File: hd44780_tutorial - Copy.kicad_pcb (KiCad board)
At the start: 2 copper layers, 157.2 x 83.5 mm, 33 parts, among them J1 LCD_2004_PinSocket_1x16_P2.54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, J2 UJC-HP-3-SMT-TR, SW1 REG SELECT, SW2 ENABLE, SW3 DS02C-254-1L-08BE

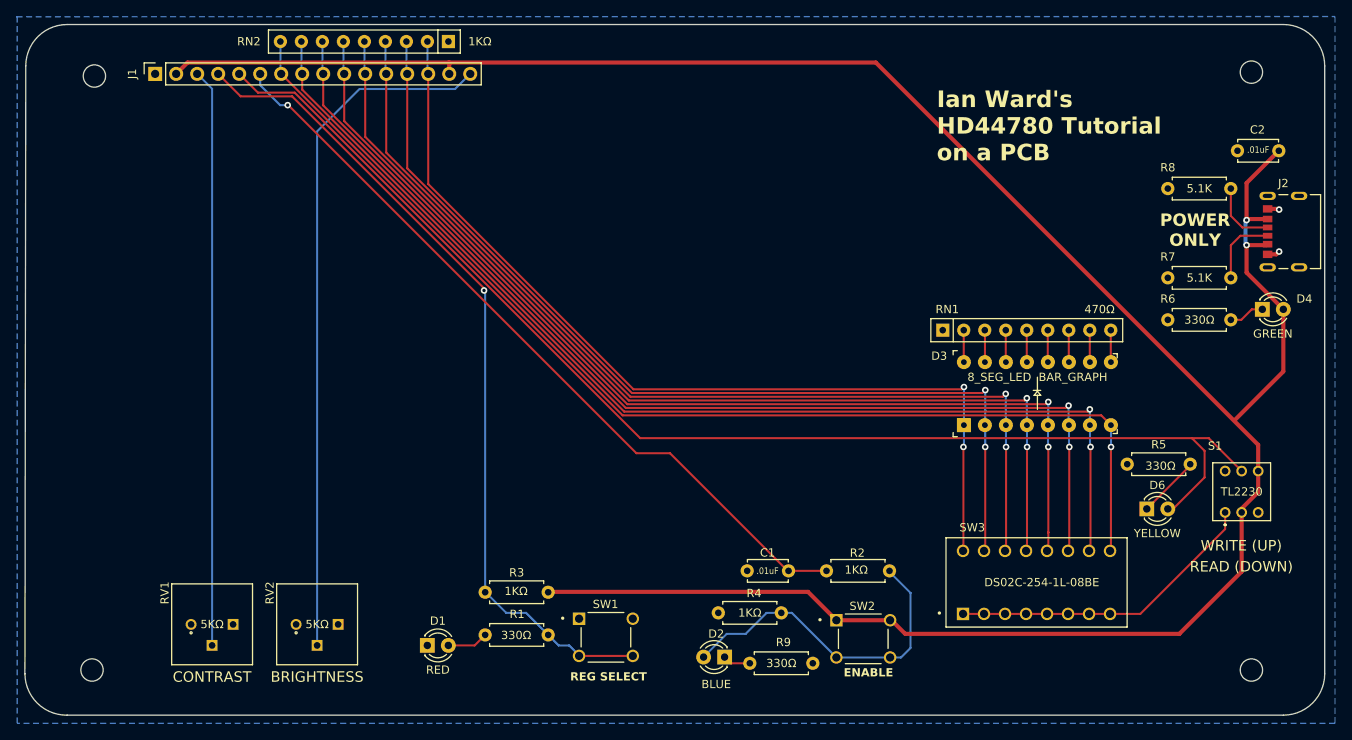
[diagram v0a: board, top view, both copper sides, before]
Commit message: Determined that adding 1K resistor to SW2 fixes the problem with this board. Created new gerber/drill files.
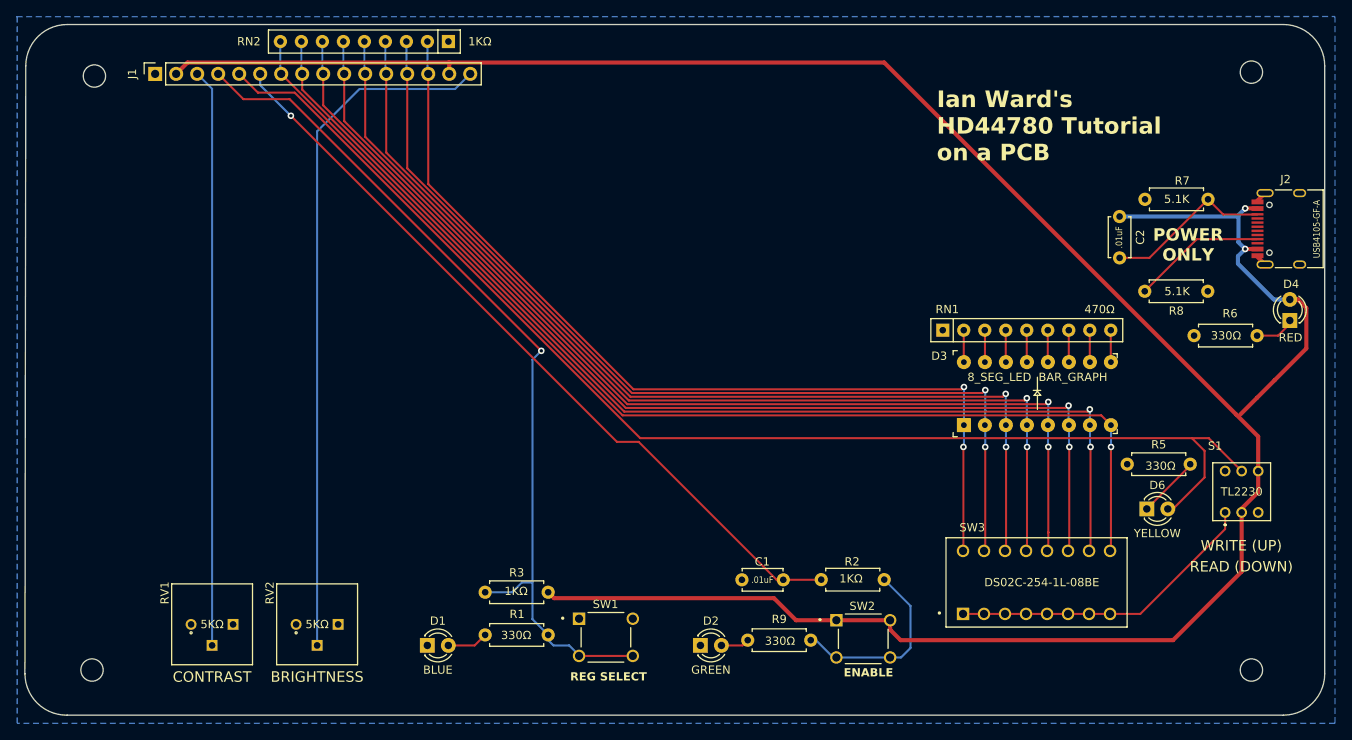
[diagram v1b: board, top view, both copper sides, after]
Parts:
- removed R4: 1KΩ, Resistor_THT:R_Axial_DIN0207_L6.3mm_D2.5mm_P7.62mm_Horizontal
- D1: value RED -> BLUE
- D2: value BLUE -> GREEN
- D4: value GREEN -> RED
- J2: value UJC-HP-3-SMT-TR -> USB4105-GF-A; footprint Lutzcraft:CUI_UJC-HP-3-SMT-TR -> footprints:USB_C_Receptacle_HRO_TYPE-C-31-M-12
- moved C2 20.8 mm to (193.6, 69.4), turned to -90 degrees
- moved R8 12.7 mm to (204.2, 78.5)
- moved R7 9.89 mm to (204.2, 67.3)
- moved R9 7.88 mm to (156.2, 120.7), turned to 180 degrees
- moved R6 3.70 mm to (202.6, 83.8)
- moved D4 3.59 mm to (214.1, 82.0), turned to 90 degrees
- moved D2 3.25 mm to (142.9, 121.3), turned to 0 degrees
- moved REF** 3.02 mm to (124.5, 80.0)
- moved J2 2.84 mm to (214.3, 70.9)
- moved C1 1.25 mm to (152.9, 113.3)
- moved R2 1.24 mm to (165.1, 113.3)
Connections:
- C2 pad 2: GND -> Net-(C2-Pad2)
- D2 pad 1: Net-(D2-K) -> GND
- J2 pad A5: Net-(J2-CC1) -> Net-(J2-PadA5)
- J2 pad B5: Net-(J2-CC2) -> Net-(C2-Pad2)
- J2 pad S1: unconnected-(J2-SHIELD-PadS1) -> GND
- R2 pad 1: Net-(D2-A) -> Net-(R2-Pad1)
- R7 pad 1: Net-(J2-CC1) -> Net-(C2-Pad2)
- R8 pad 1: Net-(J2-CC2) -> GND
- R8 pad 2: GND -> Net-(J2-PadA5)
- R9 pad 1: Net-(D2-K) -> Net-(R2-Pad1)
- R9 pad 2: GND -> Net-(D2-A)
- SW2 pad 3: Net-(D2-A) -> Net-(R2-Pad1)
- SW2 pad 4: Net-(D2-A) -> Net-(R2-Pad1)
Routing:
- net Net-(D2-A): track 40.3 -> 3.45 mm
- net Net-(R2-Pad1): track 0.00 -> 23.0 mm
- net Net-(C2-Pad2): track 0.00 -> 20.3 mm
- net Net-(J2-PadA5): track 0.00 -> 16.2 mm
- net +5V: track 300.9 -> 311.6 mm
- net Net-(J2-CC1): track 8.86 -> 0.00 mm
- net Net-(J2-CC2): track 8.33 -> 0.00 mm
- net /RS: track 100.8 -> 106.4 mm
- net Net-(D2-K): track 3.36 -> 0.00 mm
- net Net-(D4-K): track 4.34 -> 4.96 mm
- net GND: track 2.96 -> 2.74 mm, vias 2 -> 0
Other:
- board text added: "${project_name} Inspired by Ian Ward's YouTube Video: HD44780 Tutorial (https://www.youtube.com/watch?v=Gd6GUsHL4FI) PCB designed by an appreciative subscriber to his channel. Revision: ${version} 3/15/2024"
- board text removed: "${project_name} Inspired by Ian Ward's YouTube Video: HD44780 Tutorial (https://www.youtube.com/watch?v=Gd6GUsHL4FI) PCB designed by an appreciative subscriber to his channel. Revision: ${version} 3/17/2024"
